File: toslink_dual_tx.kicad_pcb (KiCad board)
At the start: 2 copper layers, 58.8 x 38.4 mm, 20 parts, among them J1 Conn_01x04_Pin, J2 Conn_01x01_Pin, U1 L7805, U2 74HC86, U3 74HC00, U4 TOTX173, U5 TOTX173

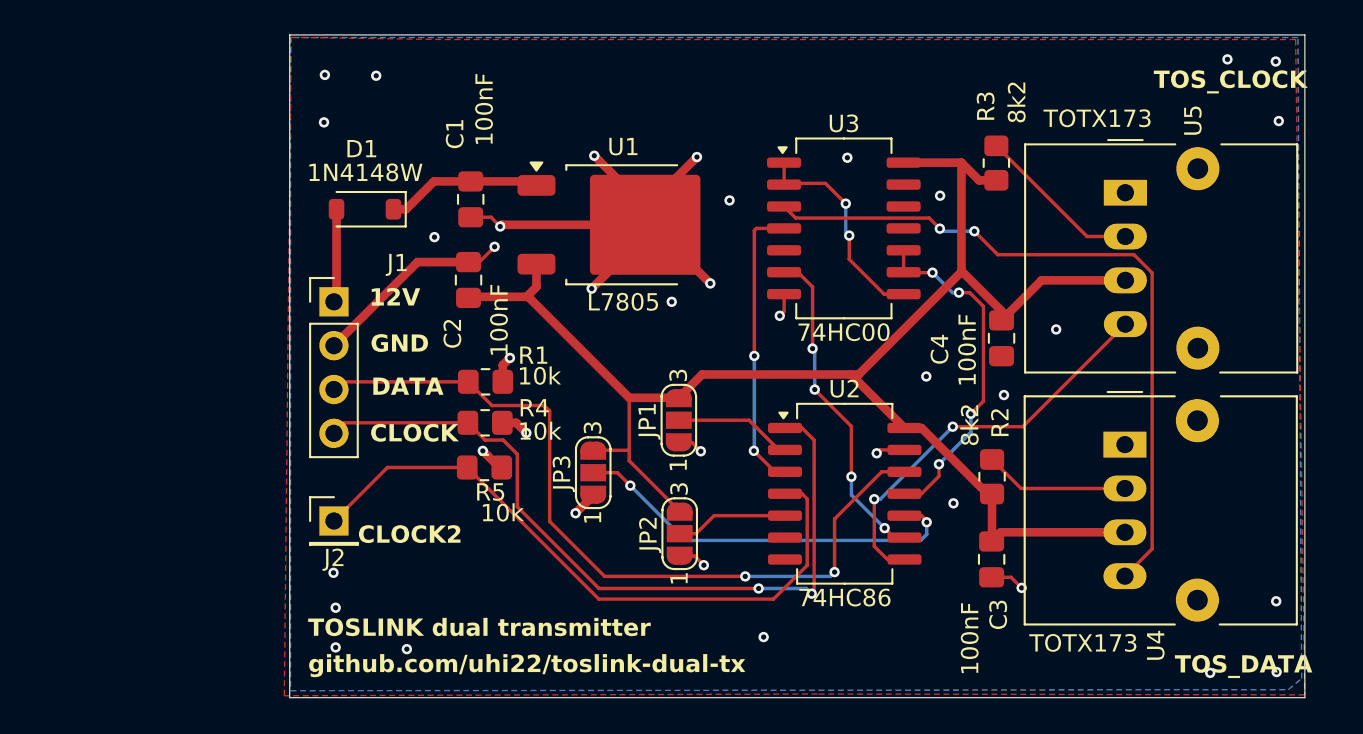
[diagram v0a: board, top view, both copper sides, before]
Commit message: added mounting holes, shrink size, added jumpers to bridge the logic gates
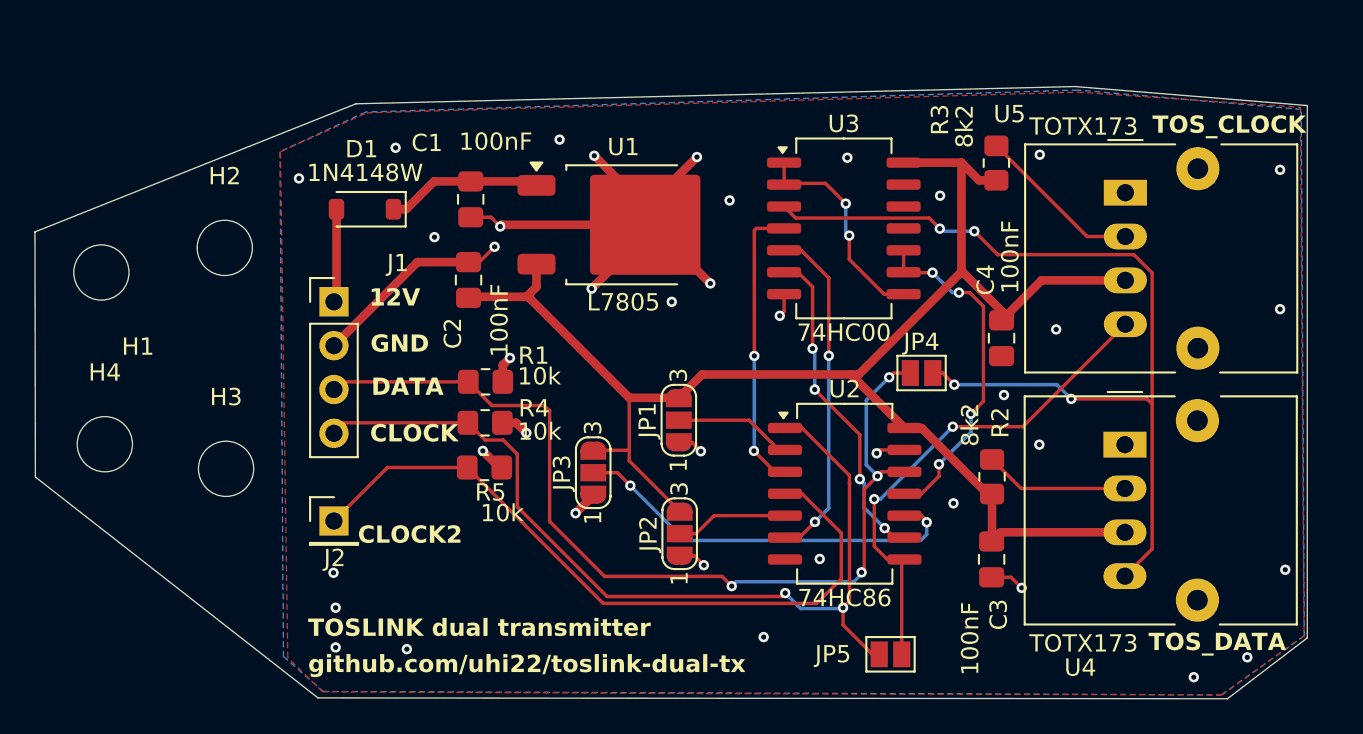
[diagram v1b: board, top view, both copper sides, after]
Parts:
- added H1: MountingHole, MountingHole:MountingHole_3.2mm_M3, F.Cu at (53.8, 73.2)
- added H2: MountingHole, MountingHole:MountingHole_3.2mm_M3, F.Cu at (60.9, 71.8)
- added H3: MountingHole, MountingHole:MountingHole_3.2mm_M3, F.Cu at (61.0, 84.6)
- added H4: MountingHole, MountingHole:MountingHole_3.2mm_M3, F.Cu at (54.0, 83.2)
- added JP4: SolderJumper_2_Open, Jumper:SolderJumper-2_P1.3mm_Open_Pad1.0x1.5mm, F.Cu at (101.3, 79.1)
- added JP5: SolderJumper_2_Open, Jumper:SolderJumper-2_P1.3mm_Open_Pad1.0x1.5mm, F.Cu at (99.5, 95.4)
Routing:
- net Net-(U2-Pad6): track 0.00 -> 19.8 mm, vias 0 -> 2
- net Net-(JP4-B): track 41.1 -> 54.6 mm, vias 2 -> 4
- net DATA: track 46.0 -> 55.3 mm, vias 2 -> 4
- net CLOCK: track 44.8 -> 52.7 mm
- net Net-(JP5-B): track 23.5 -> 29.1 mm
- net Net-(J2-Pin_1): track 37.9 -> 41.4 mm
- net GND: vias 38 -> 39
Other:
- board size 58.8 x 38.4 mm -> 73.7 x 35.5 mm

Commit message: added date on silkscreen, optimized holes
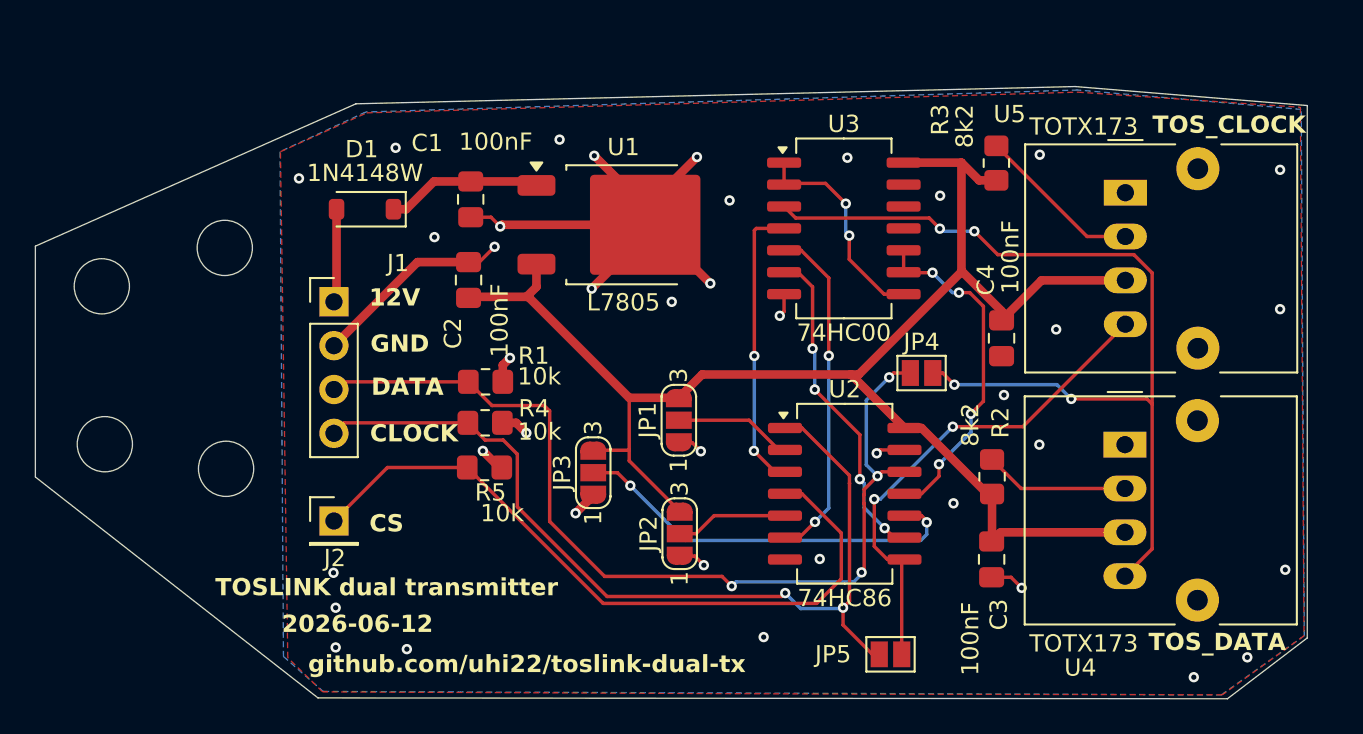
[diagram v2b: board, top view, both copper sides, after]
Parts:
- moved H1 0.80 mm to (53.8, 74.0)
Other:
- outline, holes or cut-outs redrawn
- board text added: "2026-06-12"
- board text added: "CS"
- board text removed: "CLOCK2"
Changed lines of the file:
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@@
 	(footprint "MountingHole:MountingHole_3.2mm_M3"
 		(layer "F.Cu")
-		(at 53.765 73.24)
+		(at 53.79 74.04)
 		(descr "Mounting Hole 3.2mm, M3, no annular, generated by kicad-footprint-generator mountinghole.py")
 		(tags "mountinghole M3")
 		(property "Reference" "H1"
-			(at 2.125 4.3 0)
+			(at -2.825 3.15 0)
 			(layer "F.SilkS")
+			(hide yes)
 			(effects
 				(font
@@
 			(at 0 -4.15 0)
 			(layer "F.SilkS")
+			(hide yes)
 			(effects
 				(font
@@
 			(at 0 -4.15 0)
 			(layer "F.SilkS")
+			(hide yes)
 			(effects
 				(font
@@
 			(at 0 -4.15 0)
 			(layer "F.SilkS")
+			(hide yes)
 			(effects
 				(font
@@
 		)
 		(property "Value" "Conn_01x01_Pin"
-			(at 4.525 3.975 0)
+			(at 6.2 2.8 0)
 			(layer "F.Fab")
+			(hide yes)
 			(effects
 				(font
@@
 		(pts
 			(xy 68.515 63.465) (xy 110.19 62.465) (xy 123.64 63.565) (xy 123.64 94.415) (xy 119.015 97.94) (xy 66.315 97.89)
-			(xy 49.94 85.09) (xy 49.915 70.89)
+			(xy 49.94 85.09) (xy 49.94 71.715)
 		)
 		(stroke
@@
 	)
 	(gr_text "TOSLINK dual transmitter"
-		(at 65.74 94.415 0)
+		(at 60.365 92.065 0)
 		(layer "F.SilkS")
 		(effects
@@
 		)
 	)
-	(gr_text "CLOCK2"
-		(at 68.62 89.02 0)
+	(gr_text "CS"
+		(at 69.29 88.365 0)
+		(layer "F.SilkS")
+		(effects
+			(font
+				(size 1 1)
+				(thickness 0.2)
+				(bold yes)
+			)
+			(justify left bottom)
+		)
+	)
+	(gr_text "2026-06-12"
+		(at 64.215 94.19 0)
 		(layer "F.SilkS")
 		(effects
